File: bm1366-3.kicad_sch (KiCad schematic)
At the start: 86 parts, among them U1 25MHz, U14 BM1366_mode1, U25 ADP171AUJ-R7, U26 ADP171AUJ-R7, U28 TLV3544

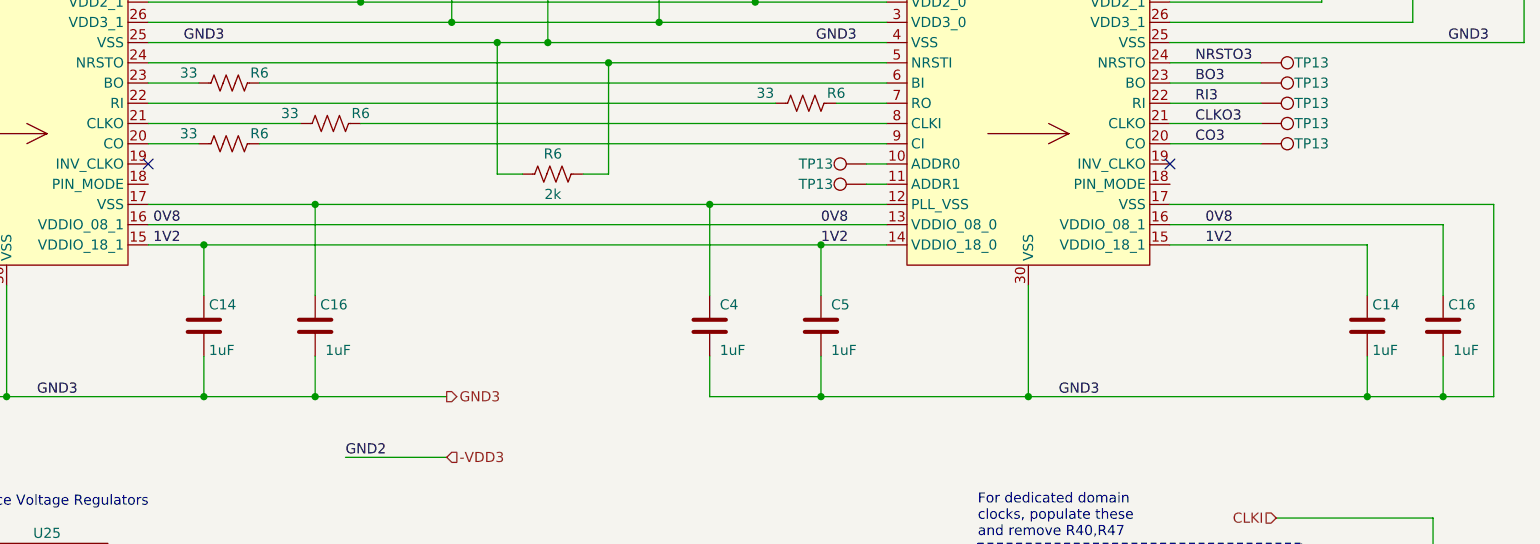
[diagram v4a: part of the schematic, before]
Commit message: routed 1366 changes
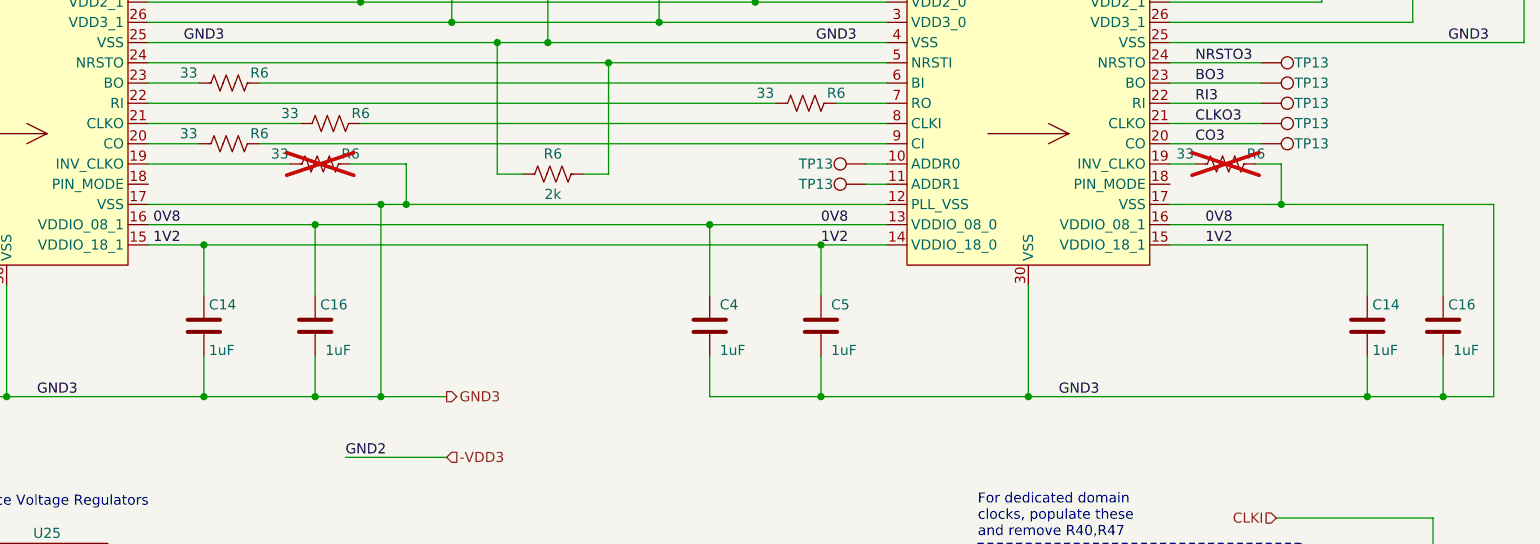
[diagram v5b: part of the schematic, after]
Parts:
- added R6 (x2): 33, Resistor_SMD:R_0402_1005Metric, symbol Device:R_US
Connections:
- net 0V8: now also C16.1, C4.1
- net GND3: now also U14.12 (PLL_VSS), U14.17 (VSS), R6.2, R6.2
- net at U14.19 (INV_CLKO): now also R6.1 (x2)
- no-connect marks 3 -> 1
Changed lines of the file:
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@@
   (junction (at 153.035 40.005) (diameter 0) (color 0 0 0 0)
   )
+  (junction (at 112.395 102.235) (diameter 0) (color 0 0 0 0)
+  )
   (junction (at 66.04 177.8) (diameter 0) (color 0 0 0 0)
   )
@@
   (junction (at 118.11 62.865) (diameter 0) (color 0 0 0 0)
   )
+  (junction (at 123.825 99.695) (diameter 0) (color 0 0 0 0)
+  )
   (junction (at 90.805 163.195) (diameter 0) (color 0 0 0 0)
   )
@@
   (junction (at 179.07 62.865) (diameter 0) (color 0 0 0 0)
   )
+  (junction (at 161.925 102.235) (diameter 0) (color 0 0 0 0)
+  )
   (junction (at 104.14 182.88) (diameter 0) (color 0 0 0 0)
   )
@@
   (junction (at 155.575 76.835) (diameter 0) (color 0 0 0 0)
   )
+  (junction (at 120.65 123.825) (diameter 0) (color 0 0 0 0)
+  )
   (junction (at 104.14 177.8) (diameter 0) (color 0 0 0 0)
   )
@@
   (junction (at 149.225 81.915) (diameter 0) (color 0 0 0 0)
   )
-  (junction (at 112.395 99.695) (diameter 0) (color 0 0 0 0)
-  )
   (junction (at 106.68 71.755) (diameter 0) (color 0 0 0 0)
   )
@@
   (junction (at 66.04 196.215) (diameter 0) (color 0 0 0 0)
   )
+  (junction (at 120.65 99.695) (diameter 0) (color 0 0 0 0)
+  )
   (junction (at 27.94 62.865) (diameter 0) (color 0 0 0 0)
   )
@@
   (junction (at 175.895 104.775) (diameter 0) (color 0 0 0 0)
   )
-  (junction (at 153.035 28.575) (diameter 0) (color 0 0 0 0)
+  (junction (at 233.68 99.695) (diameter 0) (color 0 0 0 0)
   )
-  (junction (at 161.925 99.695) (diameter 0) (color 0 0 0 0)
+  (junction (at 153.035 28.575) (diameter 0) (color 0 0 0 0)
   )
   (junction (at 176.53 42.545) (diameter 0) (color 0 0 0 0)
@@
   (junction (at 106.68 62.865) (diameter 0) (color 0 0 0 0)
   )
-  (no_connect (at 219.71 94.615))
   (no_connect (at -33.02 -21.59))
-  (no_connect (at 91.44 94.615))
   (wire (pts (xy 154.305 154.94) (xy 154.305 157.48))
     (stroke (width 0) (type solid))
@@
     (stroke (width 0) (type default))
   )
+  (wire (pts (xy 112.395 102.235) (xy 161.925 102.235))
+    (stroke (width 0) (type default))
+  )
   (wire (pts (xy 246.38 33.02) (xy 252.73 33.02))
     (stroke (width 0) (type default))
@@
     (stroke (width 0) (type default))
   )
-  (wire (pts (xy 161.925 99.695) (xy 161.925 111.125))
+  (wire (pts (xy 175.895 118.745) (xy 175.895 123.825))
     (stroke (width 0) (type default))
   )
-  (wire (pts (xy 175.895 118.745) (xy 175.895 123.825))
+  (wire (pts (xy 161.925 102.235) (xy 161.925 111.125))
     (stroke (width 0) (type default))
   )
@@
     (stroke (width 0) (type default))
   )
+  (wire (pts (xy 123.825 99.695) (xy 184.15 99.695))
+    (stroke (width 0) (type default))
+  )
   (wire (pts (xy 254 123.825) (xy 254 118.745))
     (stroke (width 0) (type default))
@@
     (stroke (width 0) (type default))
   )
-  (wire (pts (xy 112.395 111.125) (xy 112.395 99.695))
-    (stroke (width 0) (type default))
-  )
-  (wire (pts (xy 91.44 102.235) (xy 184.15 102.235))
+  (wire (pts (xy 91.44 102.235) (xy 112.395 102.235))
     (stroke (width 0) (type default))
   )
@@
     (stroke (width 0) (type default))
   )
+  (wire (pts (xy 230.505 94.615) (xy 233.68 94.615))
+    (stroke (width 0) (type default))
+  )
   (wire (pts (xy 167.64 62.865) (xy 169.545 62.865))
     (stroke (width 0) (type default))
@@
     (stroke (width 0) (type default))
   )
+  (wire (pts (xy 120.65 99.695) (xy 123.825 99.695))
+    (stroke (width 0) (type default))
+  )
   (wire (pts (xy 33.655 50.165) (xy 37.465 50.165))
     (stroke (width 0) (type default))
@@
     (stroke (width 0) (type default))
   )
+  (wire (pts (xy 116.84 94.615) (xy 123.825 94.615))
+    (stroke (width 0) (type default))
+  )
   (wire (pts (xy 154.305 147.32) (xy 154.305 144.78))
     (stroke (width 0) (type solid))
@@
     (stroke (width 0) (type default))
   )
+  (wire (pts (xy 120.65 123.825) (xy 128.905 123.825))
+    (stroke (width 0) (type default))
+  )
   (wire (pts (xy 205.105 151.13) (xy 207.645 151.13))
     (stroke (width 0) (type default))
@@
     (stroke (width 0) (type default))
   )
+  (wire (pts (xy 233.68 99.695) (xy 260.35 99.695))
+    (stroke (width 0) (type default))
+  )
   (wire (pts (xy 149.225 81.915) (xy 184.15 81.915))
     (stroke (width 0) (type default))
@@
     (stroke (width 0) (type default))
   )
-  (wire (pts (xy 112.395 123.825) (xy 128.905 123.825))
+  (wire (pts (xy 112.395 123.825) (xy 120.65 123.825))
     (stroke (width 0) (type default))
   )
@@
     (stroke (width 0) (type default))
   )
-  (wire (pts (xy 91.44 99.695) (xy 112.395 99.695))
+  (wire (pts (xy 91.44 99.695) (xy 120.65 99.695))
     (stroke (width 0) (type default))
   )
@@
     (stroke (width 0) (type default))
   )
-  (wire (pts (xy 219.71 99.695) (xy 260.35 99.695))
+  (wire (pts (xy 219.71 99.695) (xy 233.68 99.695))
     (stroke (width 0) (type default))
   )
-  (wire (pts (xy 161.925 99.695) (xy 184.15 99.695))
+  (wire (pts (xy 123.825 94.615) (xy 123.825 99.695))
+    (stroke (width 0) (type default))
+  )
+  (wire (pts (xy 120.65 99.695) (xy 120.65 123.825))
     (stroke (width 0) (type default))
   )
@@
     (stroke (width 0) (type default))
   )
+  (wire (pts (xy 219.71 94.615) (xy 222.885 94.615))
+    (stroke (width 0) (type default))
+  )
   (wire (pts (xy 59.69 158.115) (xy 59.69 163.195))
     (stroke (width 0) (type default))
@@
     (stroke (width 0) (type default))
   )
-  (wire (pts (xy 112.395 99.695) (xy 161.925 99.695))
-    (stroke (width 0) (type default))
-  )
   (wire (pts (xy 254 102.235) (xy 254 111.125))
     (stroke (width 0) (type default))
@@
     (stroke (width 0) (type default))
   )
+  (wire (pts (xy 91.44 94.615) (xy 109.22 94.615))
+    (stroke (width 0) (type default))
+  )
   (wire (pts (xy 93.345 40.005) (xy 95.25 40.005))
     (stroke (width 0) (type default))
@@
     (stroke (width 0) (type solid))
   )
+  (wire (pts (xy 161.925 102.235) (xy 184.15 102.235))
+    (stroke (width 0) (type default))
+  )
   (wire (pts (xy 88.9 144.78) (xy 104.14 144.78))
     (stroke (width 0) (type default))
@@
     (stroke (width 0) (type default))
   )
+  (wire (pts (xy 233.68 94.615) (xy 233.68 99.695))
+    (stroke (width 0) (type default))
+  )
   (wire (pts (xy 168.275 23.495) (xy 176.53 23.495))
     (stroke (width 0) (type default))
@@
     (stroke (width 0) (type default))
   )
+  (wire (pts (xy 112.395 102.235) (xy 112.395 111.125))
+    (stroke (width 0) (type default))
+  )
   (wire (pts (xy 238.76 62.865) (xy 241.3 62.865))
     (stroke (width 0) (type default))
@@
     )
   )
+  (symbol (lib_id "Device:R_US") (at 226.695 94.615 90) (unit 1)
+    (in_bom yes) (on_board yes) (dnp yes)
+    (property "Reference" "R6" (at 230.505 93.345 90)
+      (effects (font (size 1.27 1.27)))
+    )
+    (property "Value" "33" (at 221.615 93.345 90)
+      (effects (font (size 1.27 1.27)))
+    )
+    (property "Footprint" "Resistor_SMD:R_0402_1005Metric" (at 226.949 93.599 90)
+      (effects (font (size 1.27 1.27)) hide)
+    )
+    (property "Datasheet" "~" (at 226.695 94.615 0)
+      (effects (font (size 1.27 1.27)) hide)
+    )
+    (property "DK" "311-33.0LRCT-ND" (at 226.695 94.615 0)
+      (effects (font (size 1.27 1.27)) hide)
+    )
+    (property "PARTNO" "RC0402FR-0733RL" (at 226.695 94.615 0)
+      (effects (font (size 1.27 1.27)) hide)
+    )
+    (pin "1")
+    (pin "2")
+    (instances
+      (project "bm1397"
+        (path "/5ffa02c9-1f90-4b06-abee-1fc0c47a0c88"
+          (reference "R6") (unit 1)
+        )
+      )
+      (project "bitaxeHex"
+        (path "/e63e39d7-6ac0-4ffd-8aa3-1841a4541b55/4cf9c075-d009-4c35-9949-adda70ae20c7"
+          (reference "R23") (unit 1)
+        )
+        (path "/e63e39d7-6ac0-4ffd-8aa3-1841a4541b55/831c2d7c-1b0c-48f0-8d88-f1b4f08c2544"
+          (reference "R43") (unit 1)
+        )
+        (path "/e63e39d7-6ac0-4ffd-8aa3-1841a4541b55/e182566a-9202-4486-8792-212410a9233c"
+          (reference "R32") (unit 1)
+        )
+      )
+    )
+  )
   (symbol (lib_id "Device:C") (at 33.655 62.865 90) (unit 1)
     (in_bom yes) (on_board yes) (dnp no)
@@
         )
       )
+    )
+  )
+  (symbol (lib_id "Device:R_US") (at 113.03 94.615 90) (unit 1)
+    (in_bom yes) (on_board yes) (dnp yes)
+    (property "Reference" "R6" (at 116.84 93.345 90)
+      (effects (font (size 1.27 1.27)))
+    )
+    (property "Value" "33" (at 107.95 93.345 90)
+      (effects (font (size 1.27 1.27)))
+    )
+    (property "Footprint" "Resistor_SMD:R_0402_1005Metric" (at 113.284 93.599 90)
+      (effects (font (size 1.27 1.27)) hide)
+    )
+    (property "Datasheet" "~" (at 113.03 94.615 0)
+      (effects (font (size 1.27 1.27)) hide)
+    )
+    (property "DK" "311-33.0LRCT-ND" (at 113.03 94.615 0)
+      (effects (font (size 1.27 1.27)) hide)
+    )
+    (property "PARTNO" "RC0402FR-0733RL" (at 113.03 94.615 0)
+      (effects (font (size 1.27 1.27)) hide)
+    )
+    (pin "1")
+    (pin "2")
+    (instances
+      (project "bm1397"
+        (path "/5ffa02c9-1f90-4b06-abee-1fc0c47a0c88"
+          (reference "R6") (unit 1)
+        )
+      )
+      (project "bitaxeHex"
+        (path "/e63e39d7-6ac0-4ffd-8aa3-1841a4541b55/4cf9c075-d009-4c35-9949-adda70ae20c7"
+          (reference "R23") (unit 1)
+        )
+        (path "/e63e39d7-6ac0-4ffd-8aa3-1841a4541b55/831c2d7c-1b0c-48f0-8d88-f1b4f08c2544"
+          (reference "R43") (unit 1)
+        )
+        (path "/e63e39d7-6ac0-4ffd-8aa3-1841a4541b55/e182566a-9202-4486-8792-212410a9233c"
+          (reference "R23") (unit 1)
+        )
+      )

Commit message: Fix some part numbers in the BOM
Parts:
- R52, R53: DK 311-1.00LRCT-ND -> 118-CR2512-F/-1R00ELFCT-ND; PARTNO RC0402FR-071RL -> CR2512-F/-1R00ELF
- R6: DK (none) -> YAG2303CT-ND; PARTNO (none) -> RT0402BRD072KL
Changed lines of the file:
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@@
       (effects (font (size 1.27 1.27)) hide)
     )
-    (property "DK" "311-1.00LRCT-ND" (at 143.51 178.435 0)
-      (effects (font (size 1.27 1.27)) hide)
-    )
-    (property "PARTNO" "RC0402FR-071RL" (at 143.51 178.435 0)
+    (property "DK" "118-CR2512-F/-1R00ELFCT-ND" (at 143.51 178.435 0)
+      (effects (font (size 1.27 1.27)) hide)
+    )
+    (property "PARTNO" "CR2512-F/-1R00ELF" (at 143.51 178.435 0)
       (effects (font (size 1.27 1.27)) hide)
     )
@@
       (effects (font (size 1.27 1.27)) hide)
     )
-    (property "DK" "" (at 142.24 95.885 0)
-      (effects (font (size 1.27 1.27)) hide)
-    )
-    (property "PARTNO" "" (at 142.24 95.885 0)
+    (property "DK" "YAG2303CT-ND" (at 142.24 95.885 0)
+      (effects (font (size 1.27 1.27)) hide)
+    )
+    (property "PARTNO" "RT0402BRD072KL" (at 142.24 95.885 0)
       (effects (font (size 1.27 1.27)) hide)
     )
@@
       (effects (font (size 1.27 1.27)) hide)
     )
-    (property "DK" "311-1.00LRCT-ND" (at 134.62 178.435 0)
-      (effects (font (size 1.27 1.27)) hide)
-    )
-    (property "PARTNO" "RC0402FR-071RL" (at 134.62 178.435 0)
-      (effects (font (size 1.27 1.27)) hide)
-    )
+    (property "DK" "118-CR2512-F/-1R00ELFCT-ND" (at 134.62 178.435 0)
+      (effects (font (size 1.27 1.27)) hide)
+    )
+    (property "PARTNO" "CR2512-F/-1R00ELF" (at 134.62 178.435 0)
+      (effects (font (size 1.27 1.27)) hide)
+    )

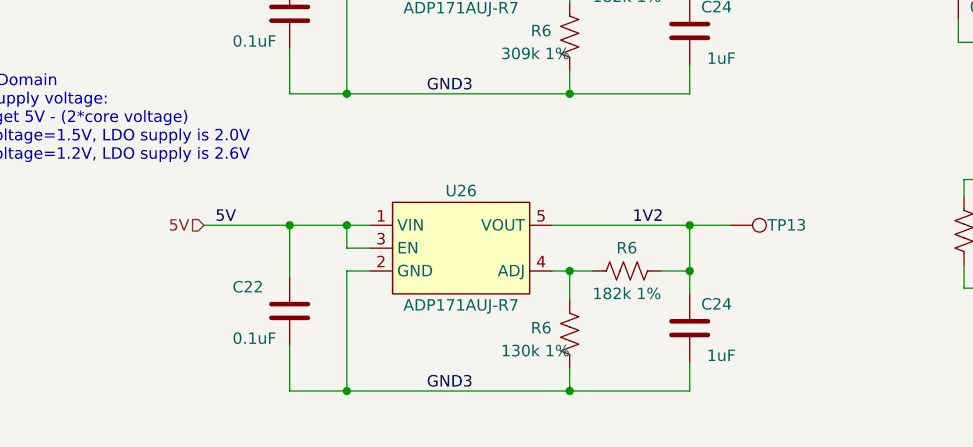
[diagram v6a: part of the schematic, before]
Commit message: add option for 1.5V ASIC Vref
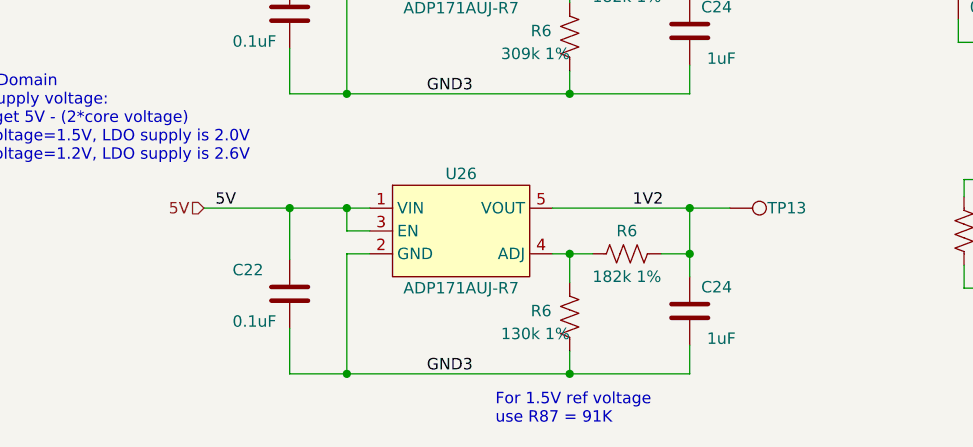
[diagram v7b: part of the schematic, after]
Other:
- note added: "For 1.5V ref voltage use R87 = 91K"
- moved on the sheet: C22, C24, R6, TP13, U26

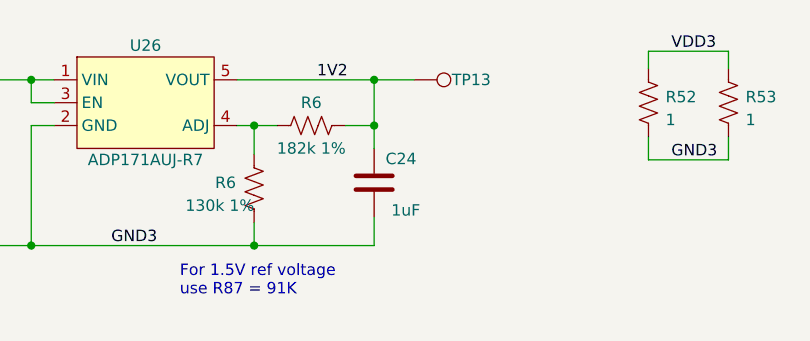
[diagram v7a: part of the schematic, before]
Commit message: add note to specify resistor value for 1.8V reference voltage
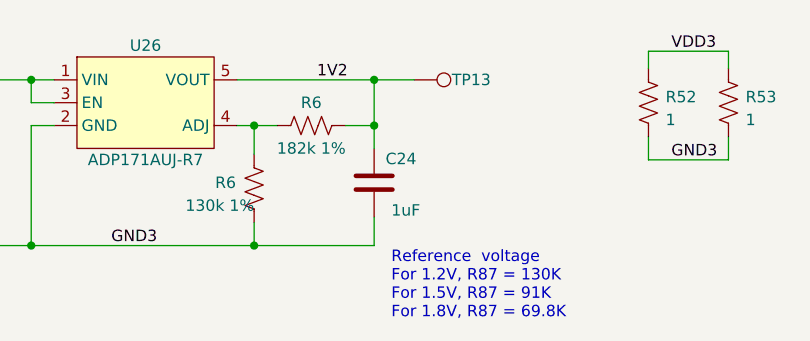
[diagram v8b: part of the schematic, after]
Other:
- note added: "Reference voltage For 1.2V, R87 = 130K For 1.5V, R87 = 91K For 1.8V, R87 = 69.8K"
- note removed: "For 1.5V ref voltage use R87 = 91K"
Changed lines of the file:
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@@
     (effects (font (size 1.27 1.27)) (justify left bottom))
   )
-  (text "For 1.5V ref voltage\nuse R87 = 91K" (at 82.55 200.025 0)
+  (text "Reference  voltage\nFor 1.2V, R87 = 130K\nFor 1.5V, R87 = 91K\nFor 1.8V, R87 = 69.8K"
+    (at 106.045 202.565 0)
     (effects (font (size 1.27 1.27)) (justify left bottom))
   )
